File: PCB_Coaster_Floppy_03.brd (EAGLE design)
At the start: 90 x 90 mm, 0 parts

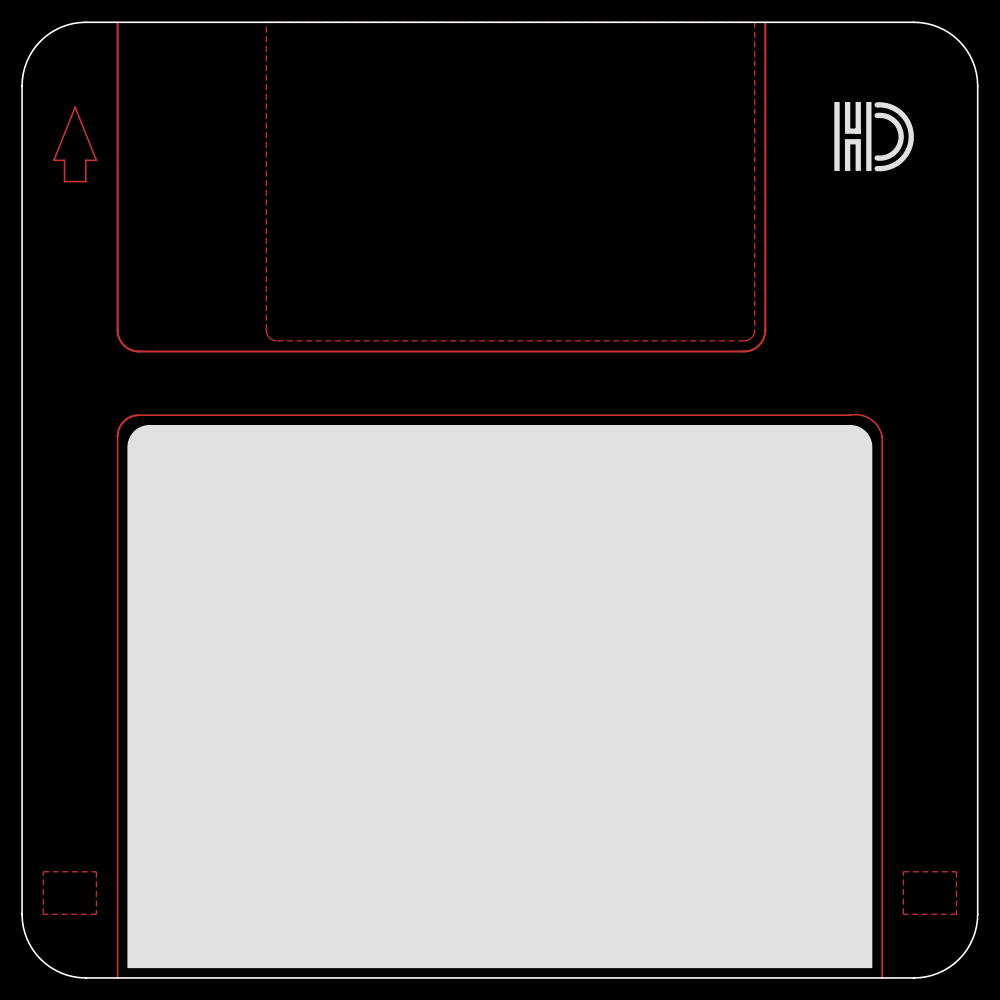
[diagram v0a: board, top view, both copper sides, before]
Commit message: updated to v3 incl stop mask
the stop mask should prevent the copper parts being covered with solder mask paint.
So they stay shiny and visible.

Also deleted older versions and single Gerber files (older Gerber ZIP remains).
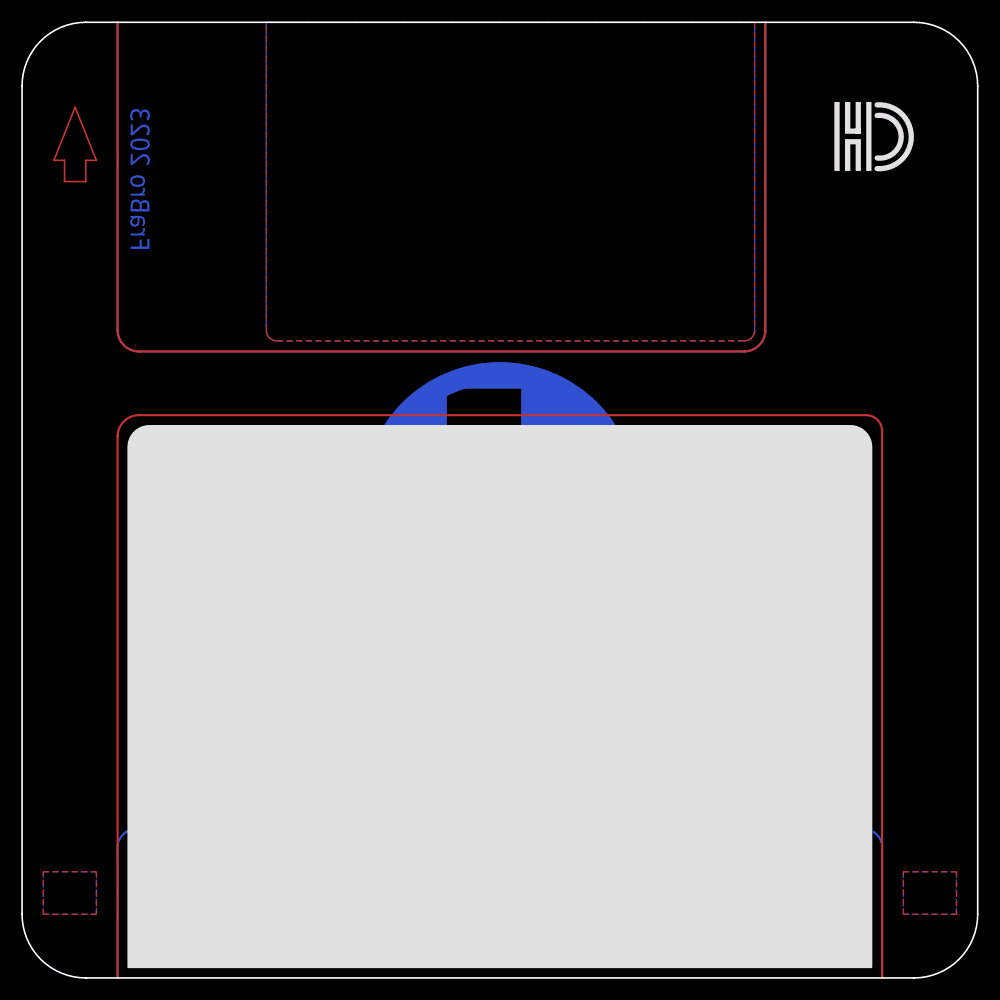
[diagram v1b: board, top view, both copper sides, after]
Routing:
- net S$2: track 120.7 -> 241.3 mm
- net S$3: track 175.4 -> 273.9 mm
- added copper zone on layer 16, net S$1
- added copper zone on layer 16, net S$6
- added copper zone on layer 16, net S$7
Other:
- board text added: "FraBro 2023"
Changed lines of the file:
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@@
 <layer number="28" name="bValues" color="7" fill="1" visible="yes" active="yes"/>
 <layer number="29" name="tStop" color="7" fill="3" visible="yes" active="yes"/>
-<layer number="30" name="bStop" color="7" fill="6" visible="no" active="yes"/>
-<layer number="31" name="tCream" color="7" fill="4" visible="no" active="yes"/>
-<layer number="32" name="bCream" color="7" fill="5" visible="no" active="yes"/>
-<layer number="33" name="tFinish" color="6" fill="3" visible="no" active="yes"/>
-<layer number="34" name="bFinish" color="6" fill="6" visible="no" active="yes"/>
-<layer number="35" name="tGlue" color="7" fill="4" visible="no" active="yes"/>
-<layer number="36" name="bGlue" color="7" fill="5" visible="no" active="yes"/>
-<layer number="37" name="tTest" color="7" fill="1" visible="no" active="yes"/>
-<layer number="38" name="bTest" color="7" fill="1" visible="no" active="yes"/>
+<layer number="30" name="bStop" color="7" fill="6" visible="yes" active="yes"/>
+<layer number="31" name="tCream" color="7" fill="4" visible="yes" active="yes"/>
+<layer number="32" name="bCream" color="7" fill="5" visible="yes" active="yes"/>
+<layer number="33" name="tFinish" color="6" fill="3" visible="yes" active="yes"/>
+<layer number="34" name="bFinish" color="6" fill="6" visible="yes" active="yes"/>
+<layer number="35" name="tGlue" color="7" fill="4" visible="yes" active="yes"/>
+<layer number="36" name="bGlue" color="7" fill="5" visible="yes" active="yes"/>
+<layer number="37" name="tTest" color="7" fill="1" visible="yes" active="yes"/>
+<layer number="38" name="bTest" color="7" fill="1" visible="yes" active="yes"/>
 <layer number="39" name="tKeepout" color="4" fill="11" visible="yes" active="yes"/>
 <layer number="40" name="bKeepout" color="1" fill="11" visible="yes" active="yes"/>
@@
 <layer number="42" name="bRestrict" color="1" fill="10" visible="yes" active="yes"/>
 <layer number="43" name="vRestrict" color="2" fill="10" visible="yes" active="yes"/>
-<layer number="44" name="Drills" color="7" fill="1" visible="no" active="yes"/>
-<layer number="45" name="Holes" color="7" fill="1" visible="no" active="yes"/>
-<layer number="46" name="Milling" color="3" fill="1" visible="no" active="yes"/>
-<layer number="47" name="Measures" color="7" fill="1" visible="no" active="yes"/>
+<layer number="44" name="Drills" color="7" fill="1" visible="yes" active="yes"/>
+<layer number="45" name="Holes" color="7" fill="1" visible="yes" active="yes"/>
+<layer number="46" name="Milling" color="3" fill="1" visible="yes" active="yes"/>
+<layer number="47" name="Measures" color="7" fill="1" visible="yes" active="yes"/>
 <layer number="48" name="Document" color="7" fill="1" visible="yes" active="yes"/>
 <layer number="49" name="Reference" color="7" fill="1" visible="yes" active="yes"/>
@@
 <dimension x1="76" y1="82.5" x2="90" y2="82.5" x3="83" y3="93" textsize="1.778" layer="48"/>
 <dimension x1="70" y1="76" x2="80" y2="76" x3="75" y3="68" textsize="1.778" layer="48"/>
+<rectangle x1="50" y1="61" x2="62" y2="86" layer="42" rot="R180"/>
+<dimension x1="76" y1="0" x2="76" y2="14" x3="100.5" y3="7" textsize="1.778" layer="48"/>
+<rectangle x1="2.5" y1="6.5" x2="6.5" y2="9.5" layer="42" rot="R180"/>
+<rectangle x1="83.5" y1="6.5" x2="87.5" y2="9.5" layer="42" rot="R180"/>
+<circle x="45" y="45" radius="13" width="0.2" layer="48"/>
+<rectangle x1="43" y1="43" x2="47" y2="47" layer="42"/>
+<circle x="45" y="45" radius="12" width="2" layer="16"/>
+<rectangle x1="34" y1="47" x2="56" y2="50.5" layer="16"/>
+<rectangle x1="34" y1="39.5" x2="56" y2="43" layer="16"/>
+<rectangle x1="43.5" y1="28.5" x2="46.5" y2="47.5" layer="16" rot="R90"/>
+<rectangle x1="33.5" y1="42.5" x2="37" y2="47.5" layer="16"/>
+<rectangle x1="53" y1="42.5" x2="56.5" y2="47.5" layer="16"/>
+<rectangle x1="43.25" y1="32.75" x2="46.75" y2="37.75" layer="16" rot="R90"/>
+<rectangle x1="40" y1="51" x2="47" y2="55.5" layer="42"/>
+<rectangle x1="50" y1="35.5" x2="53" y2="55" layer="16"/>
+<rectangle x1="53" y1="51" x2="54.5" y2="52.5" layer="16"/>
+<rectangle x1="47.5" y1="34" x2="50.5" y2="37" layer="16"/>
+<rectangle x1="47" y1="42" x2="50" y2="48" layer="16"/>
+<rectangle x1="36.5" y1="35.5" x2="40" y2="47.5" layer="16"/>
+<rectangle x1="35.5" y1="51" x2="38.5" y2="53" layer="16"/>
+<rectangle x1="37.5" y1="52.5" x2="39" y2="54" layer="16"/>
+<rectangle x1="35.5" y1="50.5" x2="38.5" y2="51" layer="16"/>
+<rectangle x1="53" y1="50.5" x2="54.5" y2="51" layer="16"/>
+<rectangle x1="41.5" y1="55.5" x2="49.5" y2="56.5" layer="16"/>
+<rectangle x1="47" y1="50.5" x2="51" y2="56" layer="16"/>
+<rectangle x1="38.5" y1="49.5" x2="40" y2="55" layer="16"/>
+<rectangle x1="38.5" y1="49.5" x2="48" y2="51" layer="16"/>
+<rectangle x1="39.5" y1="34" x2="43" y2="48" layer="16"/>
+<text x="12" y="82" size="1.778" layer="16" font="vector" rot="MR270">FraBro 2023</text>
+<polygon width="0.1524" layer="29">
+<vertex x="69.5" y="90"/>
+<vertex x="69.5" y="61" curve="-90"/>
+<vertex x="68" y="59.5"/>
+<vertex x="23.5" y="59.5" curve="-90"/>
+<vertex x="22.5" y="60.5"/>
+<vertex x="22.5" y="90.5"/>
+<vertex x="69" y="90.5" curve="-90"/>
+</polygon>
+<polygon width="0.1524" layer="30">
+<vertex x="22.5" y="90"/>
+<vertex x="22.5" y="61" curve="90"/>
+<vertex x="24" y="59.5"/>
+<vertex x="68.5" y="59.5" curve="90"/>
+<vertex x="69.5" y="60.5"/>
+<vertex x="69.5" y="90.5"/>
+<vertex x="23" y="90.5" curve="90"/>
+</polygon>
+<circle x="45" y="45" radius="13" width="0" layer="30"/>
 </plain>
 <attributes>
@@
 <vertex x="83" y="6"/>
 </polygon>
+<polygon width="0.1524" layer="16">
+<vertex x="7" y="10"/>
+<vertex x="2" y="10"/>
+<vertex x="2" y="6"/>
+<vertex x="7" y="6"/>
+</polygon>
+<polygon width="0.1524" layer="16">
+<vertex x="88" y="10"/>
+<vertex x="83" y="10"/>
+<vertex x="83" y="6"/>
+<vertex x="88" y="6"/>
+</polygon>
 </signal>
 <signal name="S$3">
-<wire x1="9" y1="0" x2="9" y2="51" width="0.1524" layer="1"/>
+<wire x1="9" y1="0" x2="9" y2="51" width="0.2" layer="1"/>
 <wire x1="9" y1="51" x2="11" y2="53" width="0.2" layer="1" curve="-90"/>
-<wire x1="11" y1="53" x2="78" y2="53" width="0.1524" layer="1"/>
-<wire x1="78" y1="53" x2="81" y2="51" width="0.1524" layer="1" curve="-90"/>
-<wire x1="81" y1="51" x2="81" y2="0" width="0.1524" layer="1"/>
+<wire x1="11" y1="53" x2="79.5" y2="53" width="0.2" layer="1"/>
+<wire x1="79.5" y1="53" x2="81" y2="51.5" width="0.2" layer="1" curve="-90"/>
+<wire x1="81" y1="51.5" x2="81" y2="0" width="0.2" layer="1"/>
+<wire x1="79" y1="14" x2="10.5" y2="14" width="0.2" layer="16"/>
+<wire x1="10.5" y1="14" x2="9" y2="12" width="0.2" layer="16" curve="90"/>
+<wire x1="81" y1="12.5" x2="79" y2="14" width="0.2" layer="16" curve="90"/>
+<wire x1="9" y1="0" x2="9" y2="12" width="0.2" layer="16"/>
+<wire x1="81" y1="0" x2="81" y2="12.5" width="0.2" layer="16"/>
+<wire x1="81" y1="0" x2="81" y2="0" width="0" layer="19" extent="1-16"/>
 </signal>
 <signal name="S$2">
@@
 <wire x1="11" y1="59" x2="9" y2="61" width="0.2" layer="1" curve="-90"/>
 <wire x1="9" y1="61" x2="9" y2="90" width="0.2" layer="1"/>
+<wire x1="70" y1="90" x2="70" y2="61" width="0.2" layer="16"/>
+<wire x1="68" y1="59" x2="70" y2="61" width="0.2" layer="16" curve="90"/>
+<wire x1="11" y1="59" x2="68" y2="59" width="0.2" layer="16"/>
+<wire x1="9" y1="61" x2="11" y2="59" width="0.2" layer="16" curve="90"/>
+<wire x1="9" y1="61" x2="9" y2="90" width="0.2" layer="16"/>
+<wire x1="70" y1="90" x2="70" y2="90" width="0" layer="19" extent="1-16"/>
 </signal>
 <signal name="S$4">
@@
 <wire x1="7" y1="77" x2="6" y2="77" width="0.1524" layer="1"/>
 </signal>
+<signal name="S$6">
+<polygon width="0.1524" layer="16">
+<vertex x="23" y="90"/>
+<vertex x="23" y="61" curve="90"/>
+<vertex x="24" y="60"/>
+<vertex x="68" y="60" curve="90"/>
+<vertex x="69" y="61"/>
+<vertex x="69" y="90"/>
+</polygon>
+</signal>
+<signal name="S$7">
+<polygon width="0.2" layer="16" orphans="yes" thermals="no" rank="5">
+<vertex x="38" y="50.5"/>
+<vertex x="52" y="50.5"/>
+<vertex x="52" y="38.5"/>
+<vertex x="38" y="38.5"/>
+</polygon>
+</signal>
 </signals>
